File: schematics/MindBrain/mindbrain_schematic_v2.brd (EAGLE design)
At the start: 81 x 47 mm, 51 parts, among them CON1 POWER, IC1 TL084, IC2 TL084

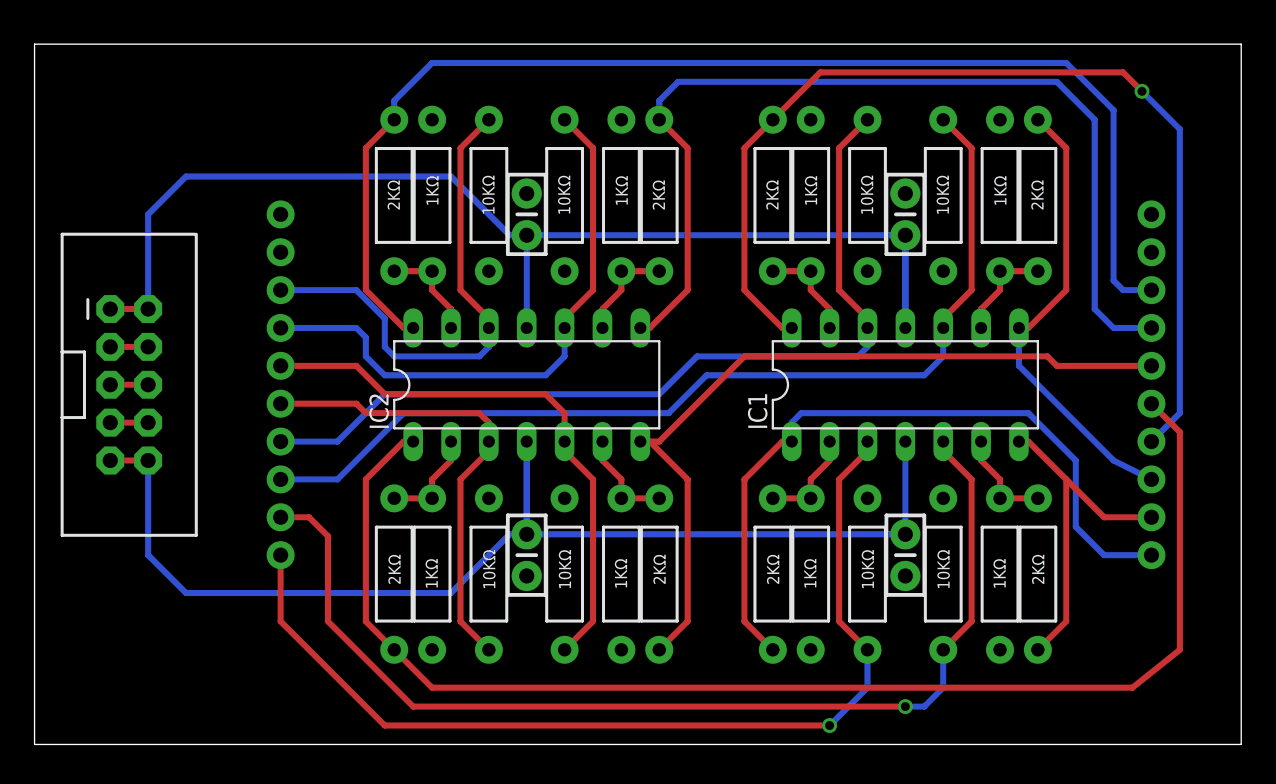
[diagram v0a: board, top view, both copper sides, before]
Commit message: added top and bottom ground pours + revision silkscreen
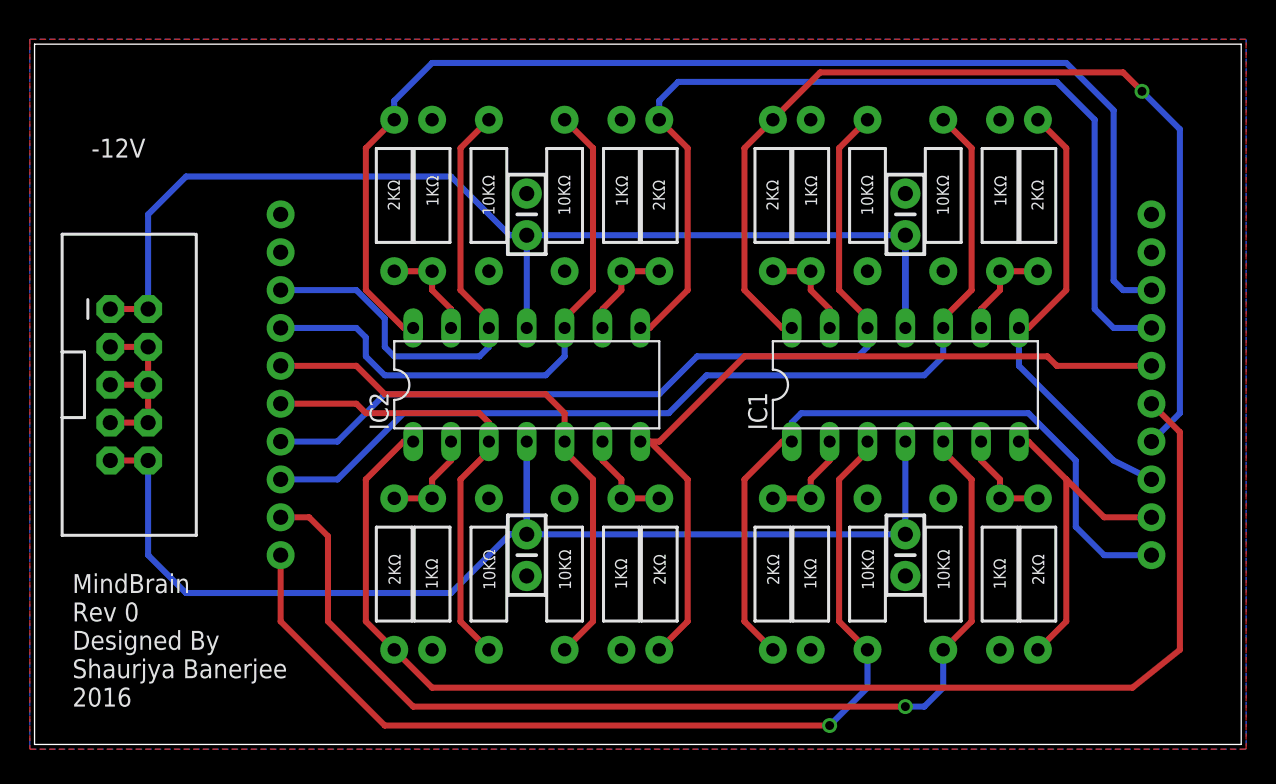
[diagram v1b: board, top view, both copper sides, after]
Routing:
- net GND: track 7.62 -> 12.7 mm
- added copper zone on layer 1, net GND
- added copper zone on layer 16, net GND
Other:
- board text added: "-12V"
- board text added: "MindBrain Rev 0 Designed By Shaurjya Banerjee 2016"

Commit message: added vias joining top and bottom ground pours
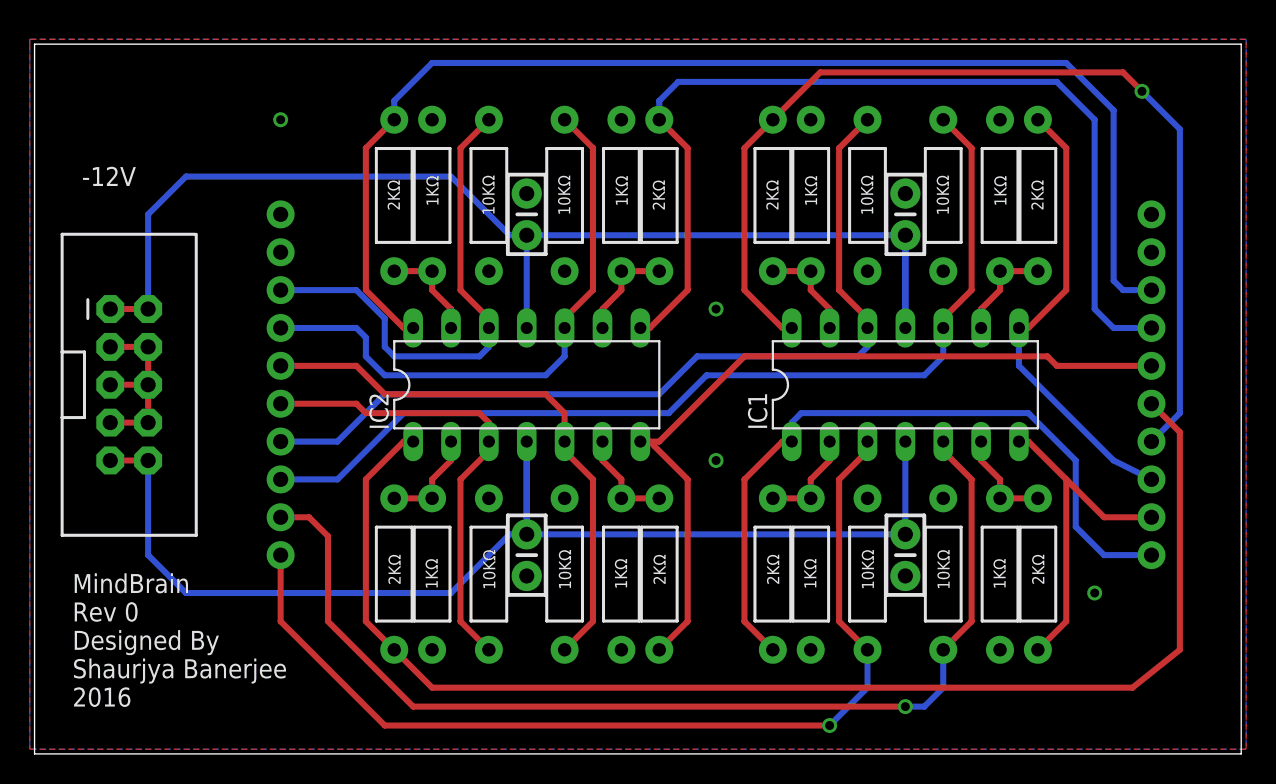
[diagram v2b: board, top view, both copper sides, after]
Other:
- board size 81 x 47 mm -> 81 x 47.6 mm
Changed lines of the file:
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@@
 <setting verticaltext="up"/>
 </settings>
-<grid distance="0.025" unitdist="inch" unit="inch" style="lines" multiple="1" display="yes" altdistance="0.0125" altunitdist="inch" altunit="inch"/>
+<grid distance="0.025" unitdist="inch" unit="inch" style="lines" multiple="1" display="no" altdistance="0.0125" altunitdist="inch" altunit="inch"/>
 <layers>
 <layer number="1" name="Top" color="4" fill="1" visible="yes" active="yes"/>
@@
 <board>
 <plain>
-<wire x1="0" y1="0" x2="80.95" y2="0" width="0" layer="20"/>
-<wire x1="80.95" y1="0" x2="80.95" y2="46.98" width="0" layer="20"/>
+<wire x1="0" y1="-0.635" x2="80.95" y2="-0.635" width="0" layer="20"/>
+<wire x1="80.95" y1="-0.635" x2="80.95" y2="46.98" width="0" layer="20"/>
 <wire x1="80.95" y1="46.98" x2="0" y2="46.98" width="0" layer="20"/>
-<wire x1="0" y1="46.98" x2="0" y2="0" width="0" layer="20"/>
+<wire x1="0" y1="46.98" x2="0" y2="-0.635" width="0" layer="20"/>
 <text x="2.54" y="2.54" size="1.27" layer="21" font="vector">MindBrain
 Rev 0
@@
 Shaurjya Banerjee
 2016</text>
-<text x="3.81" y="39.37" size="1.27" layer="21" font="vector">-12V</text>
+<text x="3.175" y="37.465" size="1.27" layer="21" font="vector">-12V</text>
 </plain>
 <attributes>
@@
 <element name="C3" library="SparkFun-Capacitors" package="CAP-PTH-SMALL-KIT" value="0.1uF" x="58.42" y="12.7" rot="R270"/>
 <element name="C4" library="SparkFun-Capacitors" package="CAP-PTH-SMALL-KIT" value="0.1uF" x="33.02" y="35.56" rot="R90"/>
-<element name="CON1" library="SparkFun-Connectors" package="2X5-SHROUDED" value="POWER" x="6.35" y="24.13" smashed="yes">
-<attribute name="VALUE" x="3.429" y="34.544" size="0.4064" layer="27" font="vector"/>
-</element>
+<element name="CON1" library="SparkFun-Connectors" package="2X5-SHROUDED" value="POWER" x="6.35" y="24.13" smashed="yes"/>
 <element name="AUDIOCARD-GND" library="SparkFun-Connectors" package="1X01NS-KIT" value="" x="16.51" y="33.02"/>
 <element name="OUTPUT-GND" library="SparkFun-Connectors" package="1X01NS-KIT" value="" x="74.93" y="33.02"/>
@@
 <wire x1="76.835" y1="22.225" x2="76.835" y2="41.275" width="0.4064" layer="16"/>
 <wire x1="76.835" y1="41.275" x2="74.295" y2="43.815" width="0.4064" layer="16"/>
-<via x="74.295" y="43.815" extent="1-16" drill="0.6" shape="octagon"/>
+<via x="74.295" y="43.815" extent="1-16" drill="0.6"/>
 <wire x1="74.295" y1="43.815" x2="73.025" y2="45.085" width="0.4064" layer="1"/>
 <wire x1="73.025" y1="45.085" x2="52.705" y2="45.085" width="0.4064" layer="1"/>
@@
 <wire x1="33.147" y1="14.097" x2="58.42" y2="14.097" width="0.4064" layer="16"/>
 </signal>
+<signal name="N$26">
+<via x="16.51" y="41.91" extent="1-16" drill="0.6"/>
+</signal>
+<signal name="N$28">
+<via x="71.12" y="10.16" extent="1-16" drill="0.6"/>
+</signal>
+<signal name="N$29">
+<via x="45.72" y="29.21" extent="1-16" drill="0.6"/>
+</signal>
+<signal name="N$30">
+<via x="45.72" y="19.05" extent="1-16" drill="0.6"/>
+</signal>
 </signals>

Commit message: getting ERC warnings, not sure why?
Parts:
- moved R3 0.64 mm to (64.8, 37.5)
- moved R4 0.64 mm to (52.1, 37.5)
- moved R7 0.64 mm to (39.4, 37.5)
- moved R8 0.64 mm to (26.7, 37.5)
- moved RF3 0.64 mm to (67.3, 37.5)
- moved RF4 0.64 mm to (49.5, 37.5)
- moved RF7 0.64 mm to (41.9, 37.5)
- moved RF8 0.64 mm to (24.1, 37.5)
- moved RIN3 0.64 mm to (61.0, 37.5)
- moved RIN4 0.64 mm to (55.9, 37.5)
- moved RIN7 0.64 mm to (35.6, 37.5)
- moved RIN8 0.64 mm to (30.5, 37.5)
- moved C1 0.64 mm to (33.0, 13.3)
- moved C3 0.64 mm to (58.4, 13.3)
- moved CON1 0.64 mm to (6.35, 24.8)
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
